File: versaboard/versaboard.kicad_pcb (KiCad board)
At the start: 4 copper layers, 57 x 43 mm, 23 parts, among them J1 UART, J39 Conn_02x20_Odd_Even, J4 DBG, J40 Conn_02x20_Odd_Even, SW1 RST, U1 ATSAML21G18B-AUT, Y1 32.768kHz

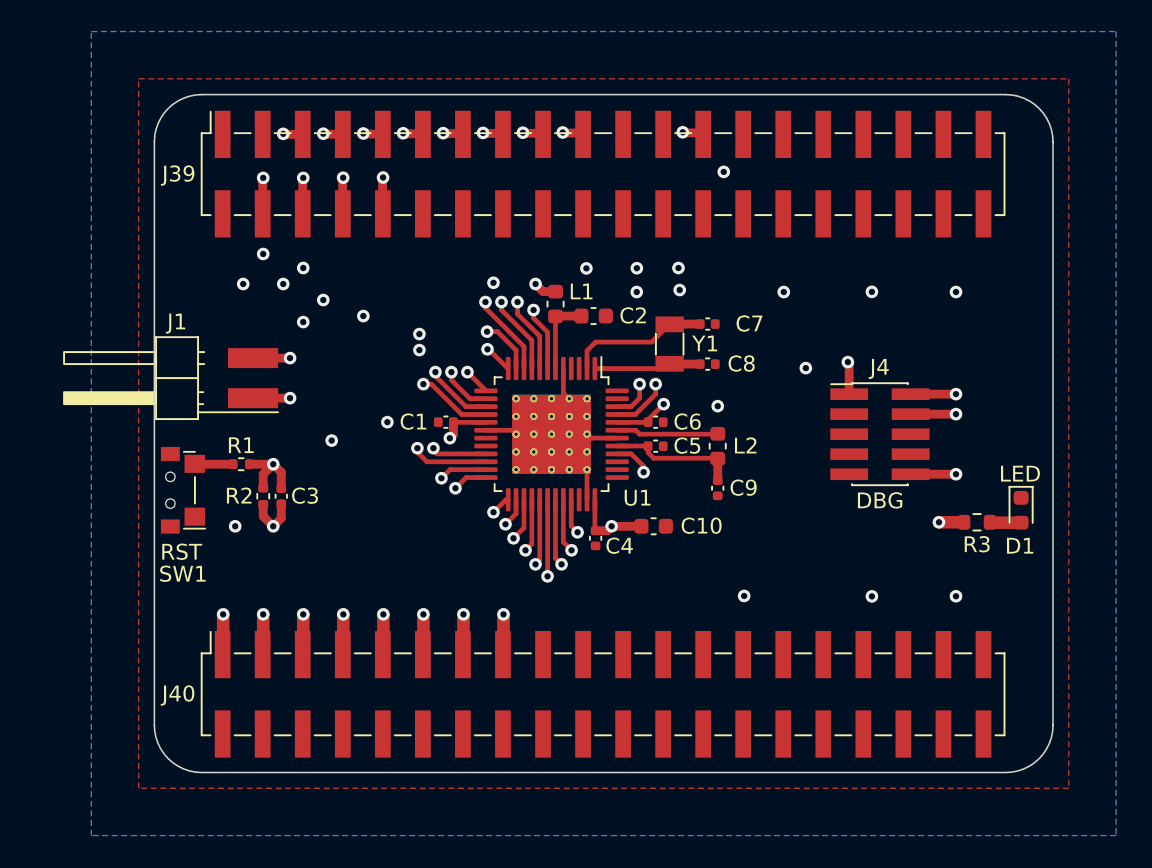
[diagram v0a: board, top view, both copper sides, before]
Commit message: versaboard: add JLCPCB mounting holes
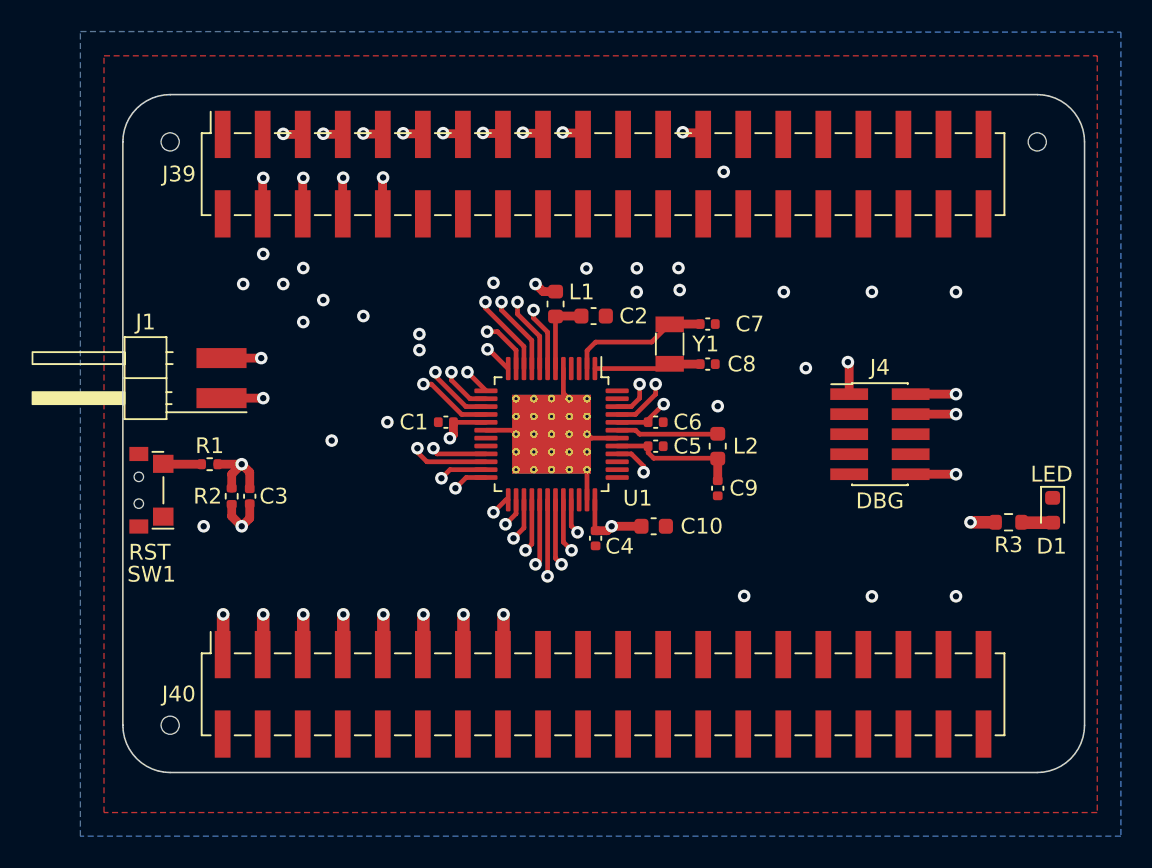
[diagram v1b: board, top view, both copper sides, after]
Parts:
- added REF**: JLCPCB_Mounting_Hole, JLCPCB:JLCPCB_Mounting_Hole, F.Cu at (88.5, 43.7)
- added REF**: JLCPCB_Mounting_Hole, JLCPCB:JLCPCB_Mounting_Hole, F.Cu at (33.5, 80.7)
- added REF**: JLCPCB_Mounting_Hole, JLCPCB:JLCPCB_Mounting_Hole, F.Cu at (33.5, 43.7)
- moved J1 2.00 mm to (31.6, 58.7)
- moved C3 2.00 mm to (38.5, 66.2)
- moved D1 2.00 mm to (89.5, 67.1)
- moved R1 2.00 mm to (36.0, 64.1)
- moved R2 2.00 mm to (37.4, 66.2)
- moved R3 2.00 mm to (86.7, 67.8)
- moved SW1 2.00 mm to (31.6, 65.8)
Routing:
- net /TX: track 23.5 -> 25.6 mm
- net /RX: track 21.4 -> 23.5 mm
- net /~{RST}: track 54.8 -> 56.8 mm
- net /LED: track 27.6 -> 29.6 mm
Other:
- board size 57 x 43 mm -> 61 x 43 mm

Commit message: versaboard: add some text
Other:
- board text added: "1"
- board text added: "2"
- board text added: "39"
- board text added: "40"
- board text added: "DBG"
- board text added: "J39"
- board text added: "J40"
- board text added: "ntcrackfpga versaboard r0001"
- board text removed: "JTAG"
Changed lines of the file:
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@@
   (gr_arc (start 91.5 80.7) (mid 90.62132 82.82132) (end 88.5 83.7) (layer "Edge.Cuts") (width 0.1))
   (gr_line (start 91.5 43.7) (end 91.5 80.7) (layer "Edge.Cuts") (width 0.1))
-  (gr_text "nc" (at 78.12795 63.383) (layer "B.SilkS")
+  (gr_text "nc" (at 78.12795 63.583 180) (layer "B.SilkS")
+    (effects (font (size 1 1) (thickness 0.15)) (justify left mirror))
+  )
+  (gr_text "ntcrackfpga\nversaboard\nr0001" (at 44.805 68.74 180) (layer "B.SilkS")
+    (effects (font (size 1 1) (thickness 0.15)) (justify mirror))
+  )
+  (gr_text "SWCK" (at 78.134619 60.97 180) (layer "B.SilkS")
+    (effects (font (size 1 1) (thickness 0.15)) (justify left mirror))
+  )
+  (gr_text "2" (at 36.75588 46.984122 180) (layer "B.SilkS")
+    (effects (font (size 1 1) (thickness 0.15)) (justify mirror))
+  )
+  (gr_text "40" (at 85.010027 46.980346 180) (layer "B.SilkS")
+    (effects (font (size 1 1) (thickness 0.15)) (justify mirror))
+  )
+  (gr_text "RESET" (at 34.483 65.669 180) (layer "B.SilkS")
+    (effects (font (size 1 1) (thickness 0.15)) (justify mirror))
+  )
+  (gr_text "UART" (at 35.5498 58.684 180) (layer "B.SilkS")
+    (effects (font (size 1 1) (thickness 0.15)) (justify mirror))
+  )
+  (gr_text "+3.3V" (at 77.758 59.7 180) (layer "B.SilkS")
     (effects (font (size 1 1) (thickness 0.15)) (justify right mirror))
   )
-  (gr_text "SWCK" (at 78.134619 60.97) (layer "B.SilkS")
+  (gr_text "GND" (at 77.754458 60.97 180) (layer "B.SilkS")
     (effects (font (size 1 1) (thickness 0.15)) (justify right mirror))
   )
-  (gr_text "RESET" (at 34.483 65.669) (layer "B.SilkS")
-    (effects (font (size 1 1) (thickness 0.15)) (justify mirror))
-  )
-  (gr_text "UART" (at 35.5498 58.684) (layer "B.SilkS")
-    (effects (font (size 1 1) (thickness 0.15)) (justify mirror))
-  )
-  (gr_text "+3.3V" (at 77.758 59.7) (layer "B.SilkS")
-    (effects (font (size 1 1) (thickness 0.15)) (justify left mirror))
-  )
-  (gr_text "GND" (at 77.754458 60.97) (layer "B.SilkS")
-    (effects (font (size 1 1) (thickness 0.15)) (justify left mirror))
-  )
-  (gr_text "nc" (at 77.741119 63.383) (layer "B.SilkS")
-    (effects (font (size 1 1) (thickness 0.15)) (justify left mirror))
+  (gr_text "nc" (at 77.741119 63.583 180) (layer "B.SilkS")
+    (effects (font (size 1 1) (thickness 0.15)) (justify right mirror))
   )
   (gr_text "←" (at 31.8414 57.414) (layer "B.SilkS")
     (effects (font (size 1 1) (thickness 0.15)) (justify mirror))
   )
-  (gr_text "GND" (at 77.747788 62.24) (layer "B.SilkS")
+  (gr_text "GND" (at 77.747788 62.24 180) (layer "B.SilkS")
+    (effects (font (size 1 1) (thickness 0.15)) (justify right mirror))
+  )
+  (gr_text "J39" (at 60.955 45.84 180) (layer "B.SilkS")
+    (effects (font (size 1 1) (thickness 0.15)) (justify mirror))
+  )
+  (gr_text "1" (at 36.79588 44.444122 180) (layer "B.SilkS")
+    (effects (font (size 1 1) (thickness 0.15)) (justify mirror))
+  )
+  (gr_text "SWDIO" (at 78.139 59.69333 180) (layer "B.SilkS")
     (effects (font (size 1 1) (thickness 0.15)) (justify left mirror))
   )
-  (gr_text "SWDIO" (at 78.139 59.69333) (layer "B.SilkS")
-    (effects (font (size 1 1) (thickness 0.15)) (justify right mirror))
+  (gr_text "nc" (at 78.12795 62.313 180) (layer "B.SilkS")
+    (effects (font (size 1 1) (thickness 0.15)) (justify left mirror))
   )
-  (gr_text "nc" (at 78.12795 62.113) (layer "B.SilkS")
-    (effects (font (size 1 1) (thickness 0.15)) (justify right mirror))
+  (gr_text "39" (at 85.043215 77.469368 180) (layer "B.SilkS")
+    (effects (font (size 1 1) (thickness 0.15)) (justify mirror))
   )
   (gr_text "→" (at 31.8414 59.954) (layer "B.SilkS")
     (effects (font (size 1 1) (thickness 0.15)) (justify mirror))
   )
-  (gr_text "nc" (at 77.741119 64.653) (layer "B.SilkS")
+  (gr_text "2" (at 36.765 80.01 180) (layer "B.SilkS")
+    (effects (font (size 1 1) (thickness 0.15)) (justify mirror))
+  )
+  (gr_text "nc" (at 77.741119 64.853 180) (layer "B.SilkS")
+    (effects (font (size 1 1) (thickness 0.15)) (justify right mirror))
+  )
+  (gr_text "39" (at 85.034095 44.44349 180) (layer "B.SilkS")
+    (effects (font (size 1 1) (thickness 0.15)) (justify mirror))
+  )
+  (gr_text "40" (at 85.019147 80.006224 180) (layer "B.SilkS")
+    (effects (font (size 1 1) (thickness 0.15)) (justify mirror))
+  )
+  (gr_text "DBG" (at 78.005 66.74 180) (layer "B.SilkS")
+    (effects (font (size 1 1) (thickness 0.15)) (justify mirror))
+  )
+  (gr_text "~{RST}" (at 78.12128 64.853 180) (layer "B.SilkS")
     (effects (font (size 1 1) (thickness 0.15)) (justify left mirror))
   )
-  (gr_text "JTAG" (at 78.805 58.24) (layer "B.SilkS")
+  (gr_text "J40" (at 60.955 78.685 180) (layer "B.SilkS")
     (effects (font (size 1 1) (thickness 0.15)) (justify mirror))
   )
-  (gr_text "~{RST}" (at 78.12128 65.034) (layer "B.SilkS")
-    (effects (font (size 1 1) (thickness 0.15)) (justify right mirror))
+  (gr_text "1" (at 36.805 77.47 180) (layer "B.SilkS")
+    (effects (font (size 1 1) (thickness 0.15)) (justify mirror))
   )
   (segment (start 60.228 62.49) (end 59.978 62.24) (width 0.3) (layer "F.Cu") (net 1))

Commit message: versaboard: increase UART arrow sizes
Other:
- board text added: "ntcrackfpga versaboard r0002"
- board text removed: "ntcrackfpga versaboard r0001"
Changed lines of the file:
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@@
     (effects (font (size 1 1) (thickness 0.15)) (justify left mirror))
   )
-  (gr_text "ntcrackfpga\nversaboard\nr0001" (at 44.805 68.74 180) (layer "B.SilkS")
+  (gr_text "ntcrackfpga\nversaboard\nr0002" (at 44.805 68.74 180) (layer "B.SilkS")
     (effects (font (size 1 1) (thickness 0.15)) (justify mirror))
   )
@@
     (effects (font (size 1 1) (thickness 0.15)) (justify right mirror))
   )
-  (gr_text "←" (at 31.8414 57.414) (layer "B.SilkS")
-    (effects (font (size 1 1) (thickness 0.15)) (justify mirror))
+  (gr_text "←" (at 32.0414 57.414) (layer "B.SilkS")
+    (effects (font (size 2 2) (thickness 0.2)) (justify mirror))
   )
   (gr_text "GND" (at 77.747788 62.24 180) (layer "B.SilkS")
@@
     (effects (font (size 1 1) (thickness 0.15)) (justify mirror))
   )
-  (gr_text "→" (at 31.8414 59.954) (layer "B.SilkS")
-    (effects (font (size 1 1) (thickness 0.15)) (justify mirror))
+  (gr_text "→" (at 32.0414 59.954) (layer "B.SilkS")
+    (effects (font (size 2 2) (thickness 0.2)) (justify mirror))
   )
   (gr_text "2" (at 36.765 80.01 180) (layer "B.SilkS")

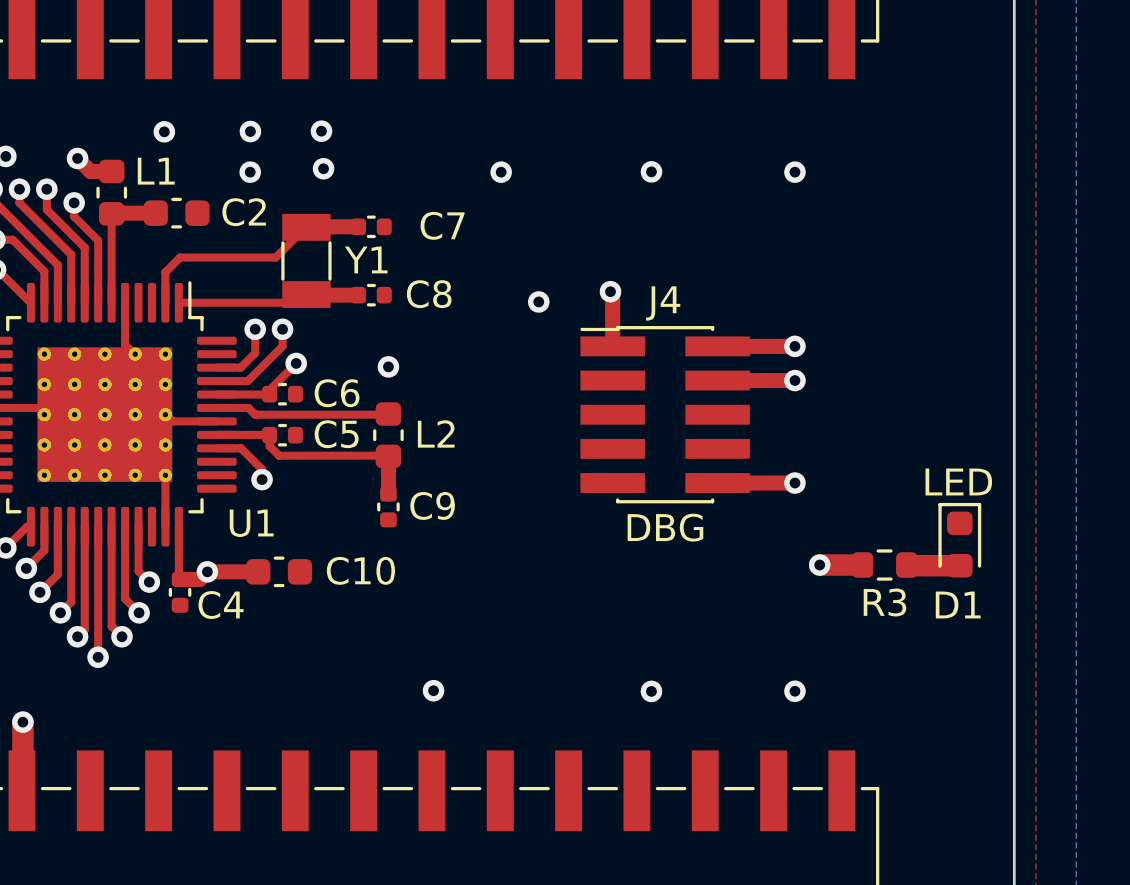
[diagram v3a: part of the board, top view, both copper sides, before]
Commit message: versaboard r0002: replace crystal with oscillator, add test points
the crystal on the test run of r0001 does not stabilize; switch to an
oscillator which should manage this without our support

also add a few test points on the board
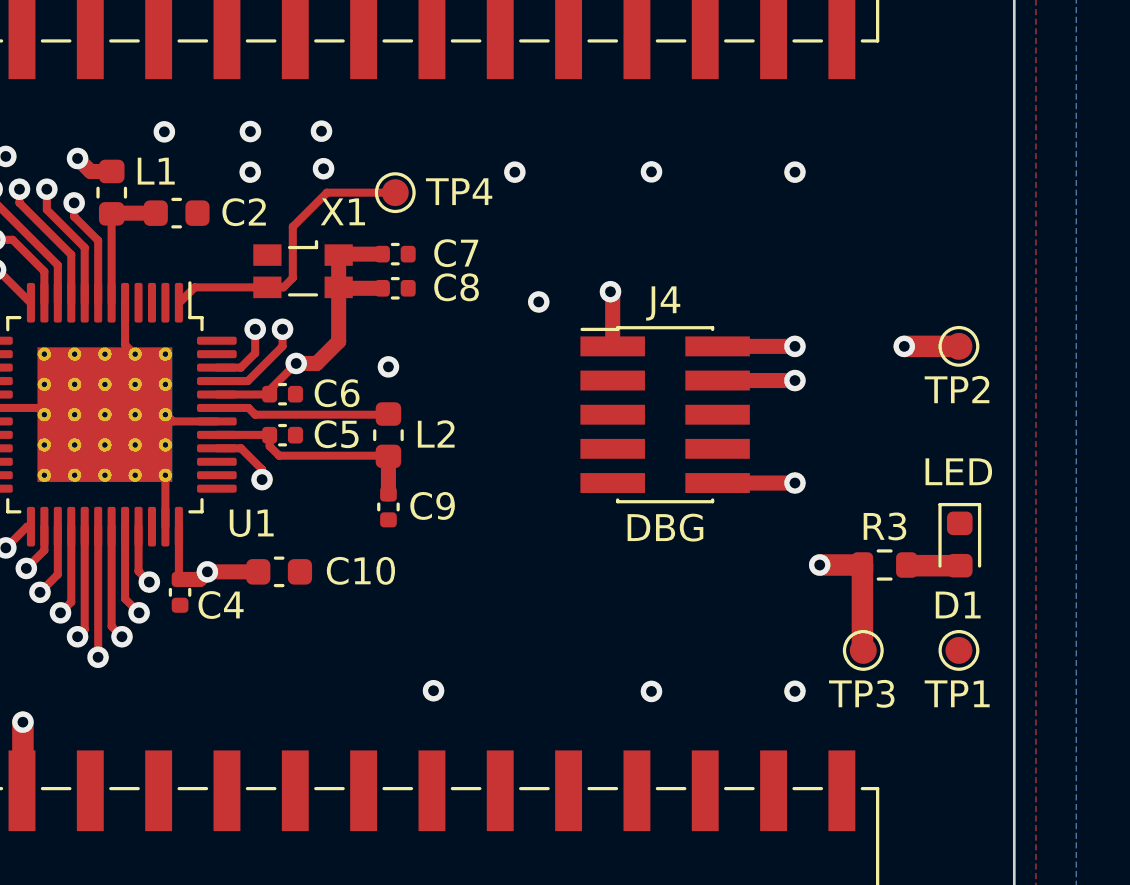
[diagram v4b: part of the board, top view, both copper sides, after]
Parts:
- removed Y1: 32.768kHz, Crystal:Crystal_SMD_3215-2Pin_3.2x1.5mm
- added TP1: TestPoint, TestPoint:TestPoint_Pad_D1.0mm, F.Cu at (89.4, 71.0)
- added TP2: TestPoint, TestPoint:TestPoint_Pad_D1.0mm, F.Cu at (89.4, 59.7)
- added TP3: TestPoint, TestPoint:TestPoint_Pad_D1.0mm, F.Cu at (85.9, 71.0)
- added TP4: TestPoint, TestPoint:TestPoint_Pad_D1.0mm, F.Cu at (68.5, 54.0)
- added X1: 32.768kHz, Oscillator:Oscillator_SMD_SeikoEpson_SG3030CM, F.Cu at (65.1, 56.9)
- C7, C8: value 22pF -> 100nF
- moved C7 1.35 mm to (68.5, 56.3), turned to 0 degrees
- moved C8 0.92 mm to (68.5, 57.5), turned to 0 degrees
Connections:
- C7 pad 1: GND -> +3.3V
- C7 pad 2: Net-(C7-Pad2) -> GND
- C8 pad 1: GND -> +3.3V
- C8 pad 2: Net-(C8-Pad2) -> GND
- U1 pad 1: Net-(C8-Pad2) -> /XIN32
- U1 pad 2: Net-(C7-Pad2) -> /XOUT32
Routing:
- net /XIN32: track 0.00 -> 10.8 mm
- net +3.3V: track 19.5 -> 29.8 mm, vias 14 -> 15
- net Net-(C7-Pad2): track 9.01 -> 0.00 mm
- net Net-(C8-Pad2): track 6.39 -> 0.00 mm
- net /LED: track 29.6 -> 32.8 mm
